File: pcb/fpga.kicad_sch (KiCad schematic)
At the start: 41 parts, among them J2 Conn_01x06, U1 ICE40HX1K-VQ100, U2 W25Q16JVZPIQ, U3 AP2127N-1.2, Y1 AMPMAFB-25.0000T

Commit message: second pcb iteration
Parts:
- removed C11, C13: 1 μF, Capacitor_SMD:C_0603_1608Metric, symbol Device:C
- removed C5: 100 nF, Capacitor_SMD:C_0603_1608Metric, symbol Device:C
- removed J2: Conn_01x06, Connector_PinSocket_1.27mm:PinSocket_1x06_P1.27mm_Vertical, symbol Connector_Generic:Conn_01x06
- removed R14: 10k, Resistor_SMD:R_0603_1608Metric, symbol Device:R
- removed R18, R19, R20, R21: 2.2k, Resistor_SMD:R_0603_1608Metric, symbol Device:R
- removed U2: W25Q16JVZPIQ, snapeda:SON127P500X600X80-9N, symbol nileswan:W25Q16JVZPIQ
- removed U3: AP2127N-1.2, Package_TO_SOT_SMD:SOT-23, symbol Regulator_Linear:AP2127N-1.2
- added R8: 2.2k, Resistor_SMD:R_0402_1005Metric, symbol Device:R
- C10, C12, C14, C15, C16, C17, C18, C19, C2, C20, C3, C4, C6, C7, C8, C9: footprint Capacitor_SMD:C_0603_1608Metric -> Capacitor_SMD:C_0402_1005Metric
- D1, D2, D3, D4, D5: footprint LED_SMD:LED_0603_1608Metric -> LED_SMD:LED_0402_1005Metric
- R11, R12, R13: value 10k -> 2.2k; footprint Resistor_SMD:R_0603_1608Metric -> Resistor_SMD:R_0402_1005Metric
- R15, R16, R17: footprint Resistor_SMD:R_0603_1608Metric -> Resistor_SMD:R_0402_1005Metric
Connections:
- net ENABLE_OUT_PSRAM is gone; now on net MBC: U1.10 (IOL_5B)
- net SD_CMD is gone; now on net /SEL: U1.16 (IOL_7B)
- net SD_DETECT is gone; now on net /IO: U1.12 (IOL_6A)
- net 3.3V: no longer R11.1, R12.1, R13.1
- net A0: now also U1.93 (IOT_87); no longer U1.72 (IOR_70)
- net A1: now also U1.94 (IOT_88); no longer U1.73 (IOR_71)
- net A16: now also U1.1 (IOL_1A); no longer U1.82 (IOT_78)
- net A17: now also U1.100 (IOT_95); no longer U1.81 (IOT_77)
- net A18: now also U1.99 (IOT_93); no longer U1.80 (IOT_75)
- net A19: now also U1.97 (IOT_91); no longer U1.79 (IOT_74)
- net A2: now also U1.95 (IOT_89); no longer U1.74 (IOR_72)
- net A3: now also U1.96 (IOT_90); no longer U1.78 (IOT_73)
- net A4: now also U1.74 (IOR_72); no longer U1.54 (IOR_55)
- net A5: now also U1.73 (IOR_71); no longer U1.53 (IOR_54)
- net A6: now also U1.72 (IOR_70); no longer U1.52 (IOR_53)
- net A7: now also U1.71 (IOR_69); no longer U1.51 (IOR_52)
- net A_HIGH0: now also U1.52 (IOR_53); no longer U1.1 (IOL_1A)
- net A_HIGH1: now also U1.53 (IOR_54); no longer U1.2 (IOL_1B)
- net A_HIGH2: now also U1.54 (IOR_55); no longer U1.3 (IOL_2A)
- net A_HIGH3: now also U1.56 (IOR_56); no longer U1.4 (IOL_2B)
- net A_HIGH4: now also U1.57 (IOR_57); no longer U1.7 (IOL_3A)
- net A_HIGH5: now also U1.59 (IOR_58); no longer U1.8 (IOL_3B)
- net D0: now also U1.91 (IOT_86); no longer U1.71 (IOR_69)
- net D1: now also U1.87 (IOT_82); no longer U1.69 (IOR_68)
- net D10: now also U1.4 (IOL_2B); no longer U1.86 (IOT_81)
- net D11: now also U1.7 (IOL_3A); no longer U1.87 (IOT_82)
- net D12: now also U1.8 (IOL_3B); no longer U1.91 (IOT_86)
- net D13: now also U1.9 (IOL_5A); no longer U1.93 (IOT_87)
- net D14: now also U1.79 (IOT_74); no longer U1.57 (IOR_57)
- net D15: now also U1.78 (IOT_73); no longer U1.56 (IOR_56)
- net D2: now also U1.86 (IOT_81); no longer U1.68 (IOR_67)
- net D3: now also U1.85 (IOT_80); no longer U1.66 (IOR_65)
- net D4: now also U1.83 (IOT_79); no longer U1.65 (IOR_64)
- net D5: now also U1.82 (IOT_78); no longer U1.64 (IOR_63)
- net D6: now also U1.81 (IOT_77); no longer U1.60 (IOR_59)
- net D7: now also U1.80 (IOT_75); no longer U1.59 (IOR_58)
- net D8: now also U1.2 (IOL_1B); no longer U1.83 (IOT_79)
- net D9: now also U1.3 (IOL_2A); no longer U1.85 (IOT_80)
- net GND: now also R11.1, R12.1, R13.1, R15.1, R8.1; no longer R15.2
- net MBC: no longer U1.94 (IOT_88)
- net SCLK: now also U1.15 (IOL_7A_GBIN6); no longer U1.89 (IOT_84_GBIN1)
- net /IO: no longer U1.95 (IOT_89)
- net /OE: now also U1.90 (IOT_85_GBIN0); no longer U1.96 (IOT_90)
- net /SEL: no longer U1.99 (IOT_93)
- net /SEL_PSRAM: now also U1.65 (IOR_64); no longer U1.9 (IOL_5A)
- net /WE: now also U1.13 (IOL_6B_GBIN7); no longer U1.97 (IOT_91)
- net at D4.1 (K): now also R12.2
- net at D4.2 (A): now also U1.28 (IOB_28); no longer U1.24 (IOL_12A)
- net at D5.1 (K): now also R13.2
- net at D5.2 (A): now also U1.29 (IOB_29); no longer U1.25 (IOL_12B)
- net at D3.1 (K): now also R11.2
- net FLASH_PICO: now reaches U1.45 (IOB_44_SDO)
- net FLASH_POCI: now reaches U1.46 (IOB_45_SDI)
- net FLASH_CLK: now reaches U1.48 (IOB_46_SCK)
- net FLASH_CLK: no longer R11.2
- net FLASH_CS: now reaches U1.49 (IOB_47_SS)
- net FLASH_CS: no longer R13.2
- net at D2.2 (A): now also U1.26 (IOB_26); no longer U1.20 (IOL_10A)
- net at D3.2 (A): now also U1.27 (IOB_27); no longer U1.21 (IOL_10B)
- net at D2.1 (K): now also R8.2
- net 1.2V: now reaches C14.1, C15.1, C17.1, C19.1, U1.11 (VCC), U1.35 (VCC), U1.61 (VCC), U1.77 (VCC)
- net at U1.34 (IOB_36_GBIN4): now also Y1.3 (OUTPUT); no longer Y1.1 (OE/STBY)
- net at U1.36 (IOB_34): now also Y1.1 (OE/STBY); no longer Y1.3 (OUTPUT)
- net CRESET_B: now reaches R17.2, U1.44 (CRESET_B)
- net at D1.1 (K): now also R15.2; no longer R15.1
- net SD_CLK renamed TF_SEL
- net SD_DAT0 renamed TF_POW
- new net A8: U1.69 (IOR_68)
- new net A_HIGH6: U1.60 (IOR_59)
- new net TF_CLK: U1.21 (IOL_10B)
- new net TF_DETECT: U1.25 (IOL_12B)
- new net TF_PICO: U1.20 (IOL_10A)
- new net TF_POCI: U1.24 (IOL_12A)
- new net /PSRAM_LB: U1.68 (IOR_67)
- new net /PSRAM_UB: U1.66 (IOR_65)
- new net /SEL_SRAM: U1.64 (IOR_63)
- no-connect marks 17 -> 11
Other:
- note added: "Core power"
- moved on the sheet: C10, C12, C14, C15, C17, C19, C2, C3, C4, C6, C7, C8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

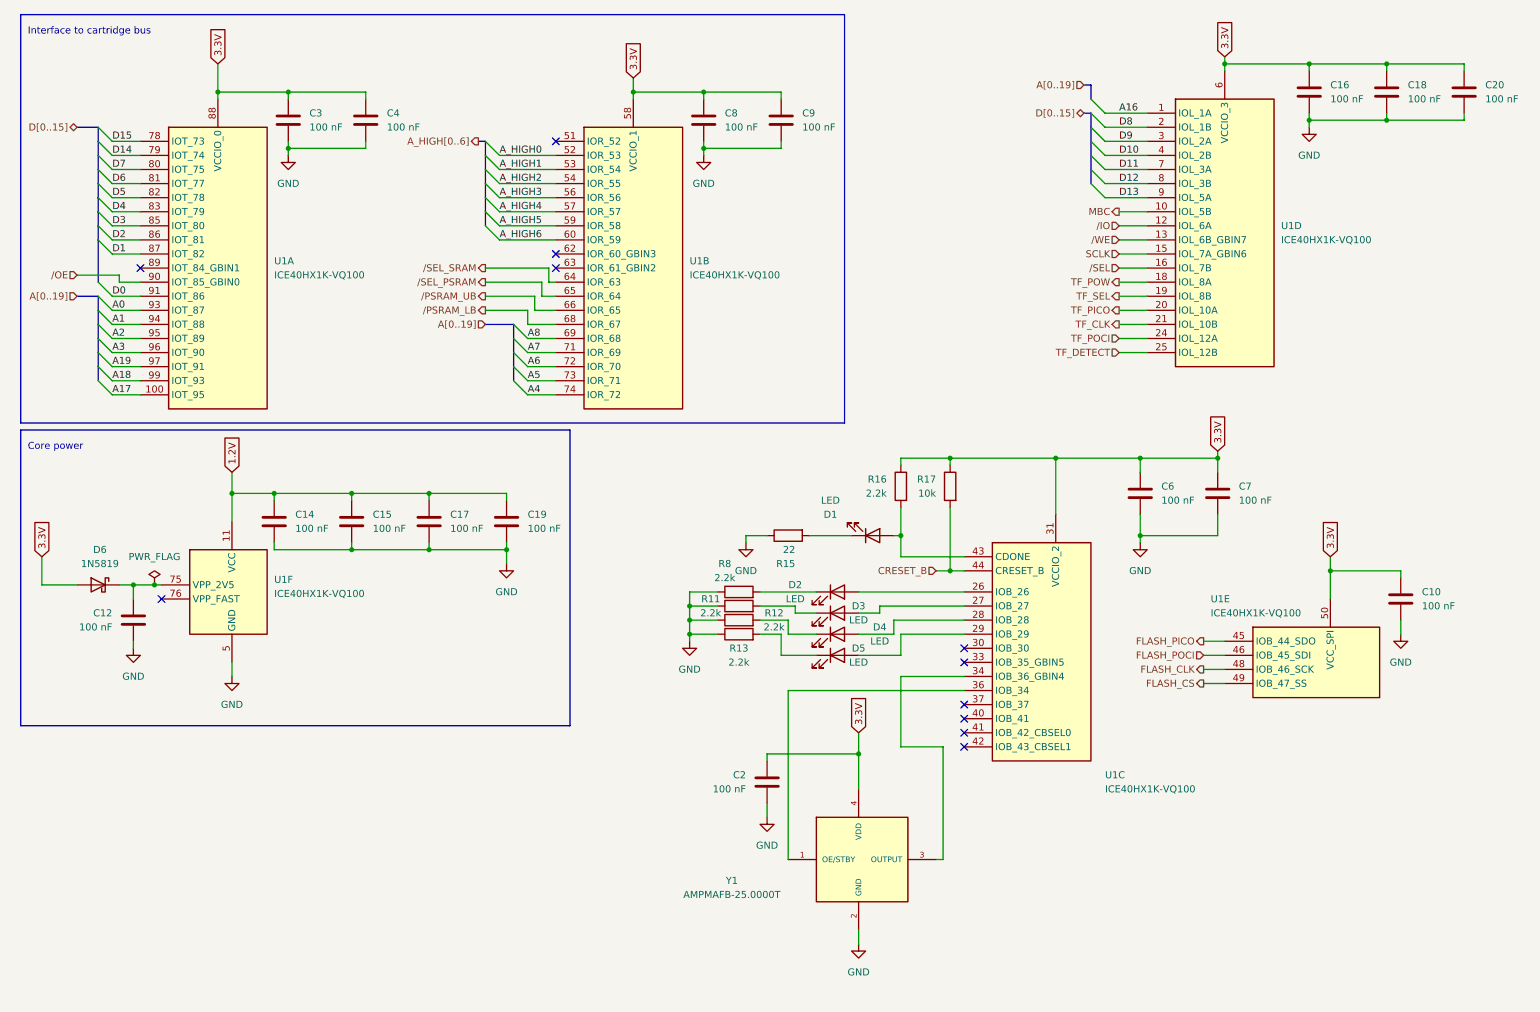
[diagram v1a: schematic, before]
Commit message: pcb revision 3 and 16 MB PSRAM support
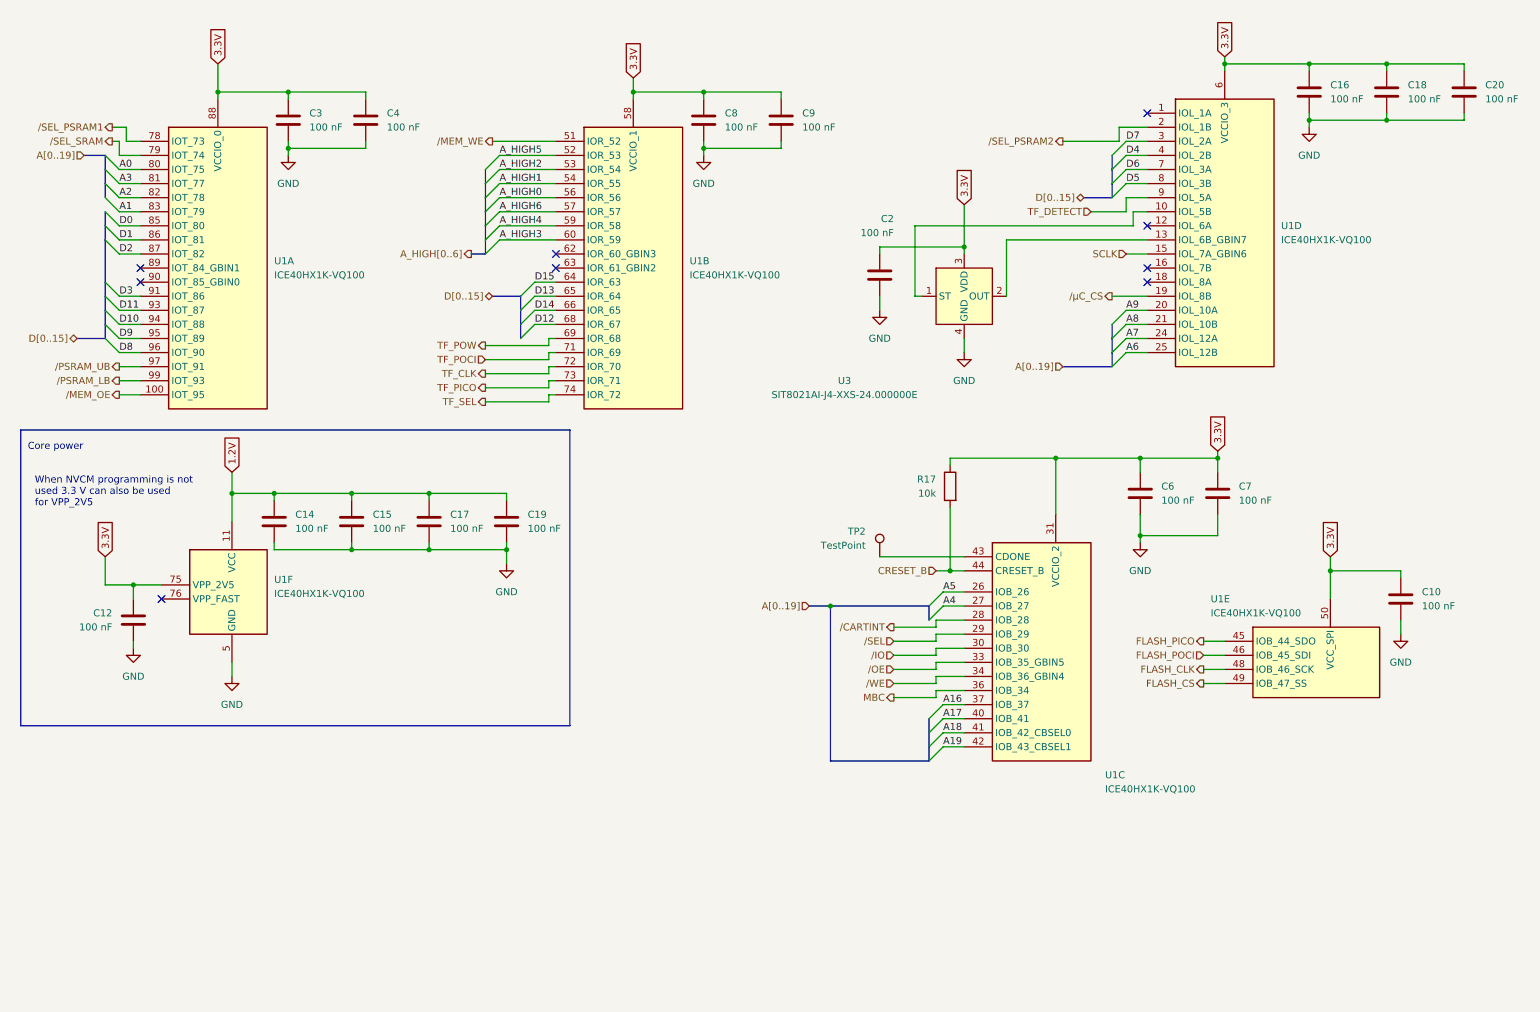
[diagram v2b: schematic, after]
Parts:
- removed D1, D2, D3, D4, D5: LED, LED_SMD:LED_0402_1005Metric, symbol Device:LED
- removed D6: 1N5819, Diode_SMD:D_SOD-123, symbol Diode:1N5819
- removed R11, R12, R13, R16, R8: 2.2k, Resistor_SMD:R_0402_1005Metric, symbol Device:R
- removed R15: 22, Resistor_SMD:R_0402_1005Metric, symbol Device:R
- removed Y1: AMPMAFB-25.0000T, snapeda:XTAL_AMPMAFB-25.0000T, symbol AMPMAFB-25.0000T:AMPMAFB-25.0000T
- added TP2: TestPoint, TestPoint:TestPoint_Pad_D1.0mm, symbol Connector:TestPoint
- added U3: SIT8021AI-J4-XXS-24.000000E, snapeda:BGA4N41X100P2X2_84X154X60N, symbol nileswan:SIT8021AI-J4-XXS-24.000000E
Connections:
- net /SEL_PSRAM is gone; now on net D13: U1.65 (IOR_64)
- net 3.3V: now also C12.1, U1.75 (VPP_2V5), U3.3 (VDD)
- net A0: now also U1.80 (IOT_75); no longer U1.93 (IOT_87)
- net A1: now also U1.83 (IOT_79); no longer U1.94 (IOT_88)
- net A16: now also U1.37 (IOB_37); no longer U1.1 (IOL_1A)
- net A17: now also U1.40 (IOB_41); no longer U1.100 (IOT_95)
- net A18: now also U1.41 (IOB_42_CBSEL0); no longer U1.99 (IOT_93)
- net A19: now also U1.42 (IOB_43_CBSEL1); no longer U1.97 (IOT_91)
- net A2: now also U1.82 (IOT_78); no longer U1.95 (IOT_89)
- net A3: now also U1.81 (IOT_77); no longer U1.96 (IOT_90)
- net A4: now also U1.27 (IOB_27); no longer U1.74 (IOR_72)
- net A5: now also U1.26 (IOB_26); no longer U1.73 (IOR_71)
- net A6: now also U1.25 (IOL_12B); no longer U1.72 (IOR_70)
- net A7: now also U1.24 (IOL_12A); no longer U1.71 (IOR_69)
- net A8: now also U1.21 (IOL_10B); no longer U1.69 (IOR_68)
- net A_HIGH0: now also U1.56 (IOR_56); no longer U1.52 (IOR_53)
- net A_HIGH1: now also U1.54 (IOR_55); no longer U1.53 (IOR_54)
- net A_HIGH2: now also U1.53 (IOR_54); no longer U1.54 (IOR_55)
- net A_HIGH3: now also U1.60 (IOR_59); no longer U1.56 (IOR_56)
- net A_HIGH4: now also U1.59 (IOR_58); no longer U1.57 (IOR_57)
- net A_HIGH5: now also U1.52 (IOR_53); no longer U1.59 (IOR_58)
- net A_HIGH6: now also U1.57 (IOR_57); no longer U1.60 (IOR_59)
- net D0: now also U1.85 (IOT_80); no longer U1.91 (IOT_86)
- net D1: now also U1.86 (IOT_81); no longer U1.87 (IOT_82)
- net D10: now also U1.94 (IOT_88); no longer U1.4 (IOL_2B)
- net D11: now also U1.93 (IOT_87); no longer U1.7 (IOL_3A)
- net D12: now also U1.68 (IOR_67); no longer U1.8 (IOL_3B)
- net D13: no longer U1.9 (IOL_5A)
- net D14: now also U1.66 (IOR_65); no longer U1.79 (IOT_74)
- net D15: now also U1.64 (IOR_63); no longer U1.78 (IOT_73)
- net D2: now also U1.87 (IOT_82); no longer U1.86 (IOT_81)
- net D3: now also U1.91 (IOT_86); no longer U1.85 (IOT_80)
- net D4: now also U1.4 (IOL_2B); no longer U1.83 (IOT_79)
- net D5: now also U1.8 (IOL_3B); no longer U1.82 (IOT_78)
- net D6: now also U1.7 (IOL_3A); no longer U1.81 (IOT_77)
- net D7: now also U1.3 (IOL_2A); no longer U1.80 (IOT_75)
- net D8: now also U1.96 (IOT_90); no longer U1.2 (IOL_1B)
- net D9: now also U1.95 (IOT_89); no longer U1.3 (IOL_2A)
- net GND: now also U3.4 (GND)
- net MBC: now also U1.36 (IOB_34); no longer U1.10 (IOL_5B)
- net TF_CLK: now also U1.72 (IOR_70); no longer U1.21 (IOL_10B)
- net TF_DETECT: now also U1.9 (IOL_5A); no longer U1.25 (IOL_12B)
- net TF_PICO: now also U1.73 (IOR_71); no longer U1.20 (IOL_10A)
- net TF_POCI: now also U1.71 (IOR_69); no longer U1.24 (IOL_12A)
- net TF_POW: now also U1.69 (IOR_68); no longer U1.18 (IOL_8A)
- net TF_SEL: now also U1.74 (IOR_72); no longer U1.19 (IOL_8B)
- net /IO: now also U1.30 (IOB_30); no longer U1.12 (IOL_6A)
- net /OE: now also U1.33 (IOB_35_GBIN5); no longer U1.90 (IOT_85_GBIN0)
- net /PSRAM_LB: now also U1.99 (IOT_93); no longer U1.68 (IOR_67)
- net /PSRAM_UB: now also U1.97 (IOT_91); no longer U1.66 (IOR_65)
- net /SEL: now also U1.29 (IOB_29); no longer U1.16 (IOL_7B)
- net /SEL_SRAM: now also U1.79 (IOT_74); no longer U1.64 (IOR_63)
- net /WE: now also U1.34 (IOB_36_GBIN4); no longer U1.13 (IOL_6B_GBIN7)
- net /MEM_WE: now reaches U1.51 (IOR_52)
- net /CARTINT: now reaches U1.28 (IOB_28)
- net at U1.43 (CDONE): now also TP2.1
- new net: U1.10 (IOL_5B), U3.1 (ST)
- new net: U1.13 (IOL_6B_GBIN7), U3.2 (OUT)
- new net A9: U1.20 (IOL_10A)
- new net /MEM_OE: U1.100 (IOT_95)
- new net /SEL_PSRAM1: U1.78 (IOT_73)
- new net /SEL_PSRAM2: U1.2 (IOL_1B)
- new net /μC_CS: U1.19 (IOL_8B)
- no-connect marks 11 -> 9
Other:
- note added: "When NVCM programming is not used 3.3 V can also be used for VPP_2V5"
- note removed: "Interface to cartridge bus"
